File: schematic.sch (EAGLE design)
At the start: 32 parts, among them IC1 PIC16F877P, T1 2N2222, T2 2N2222

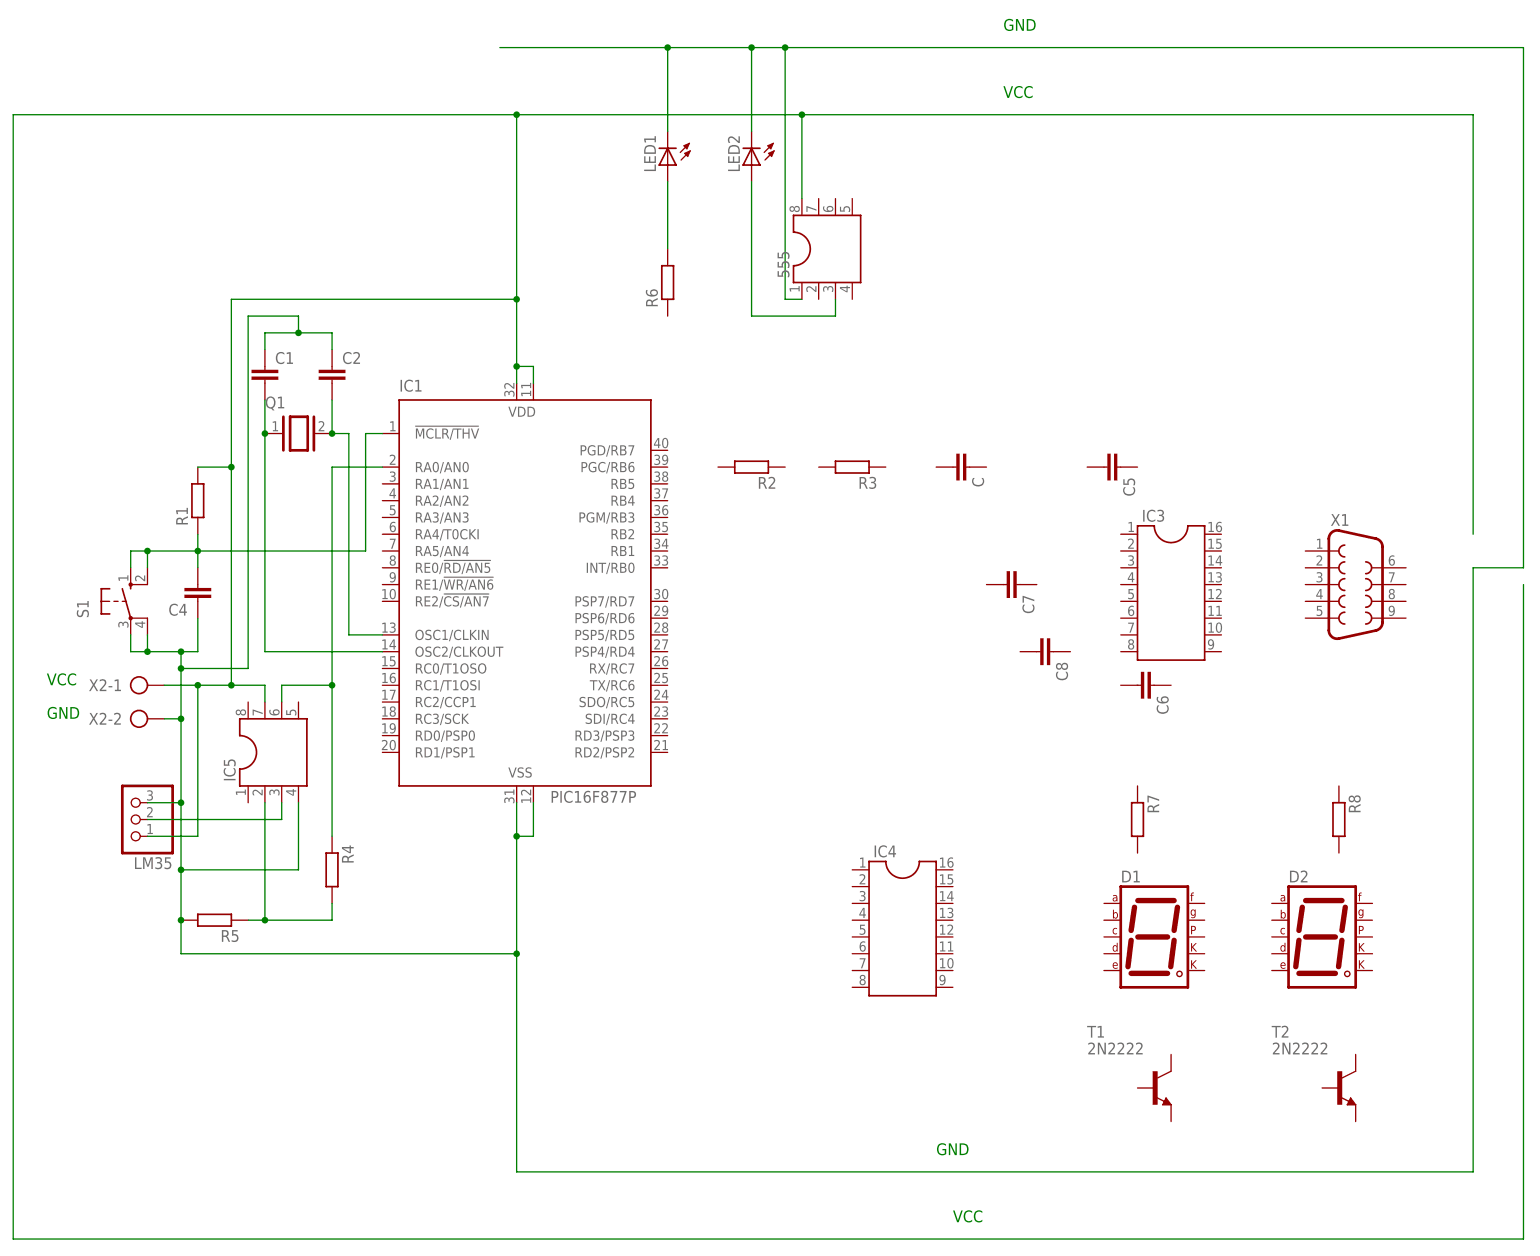
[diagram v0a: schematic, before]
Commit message: choix final du modele du pic + ajout de 4 condo max232 + suite schéma
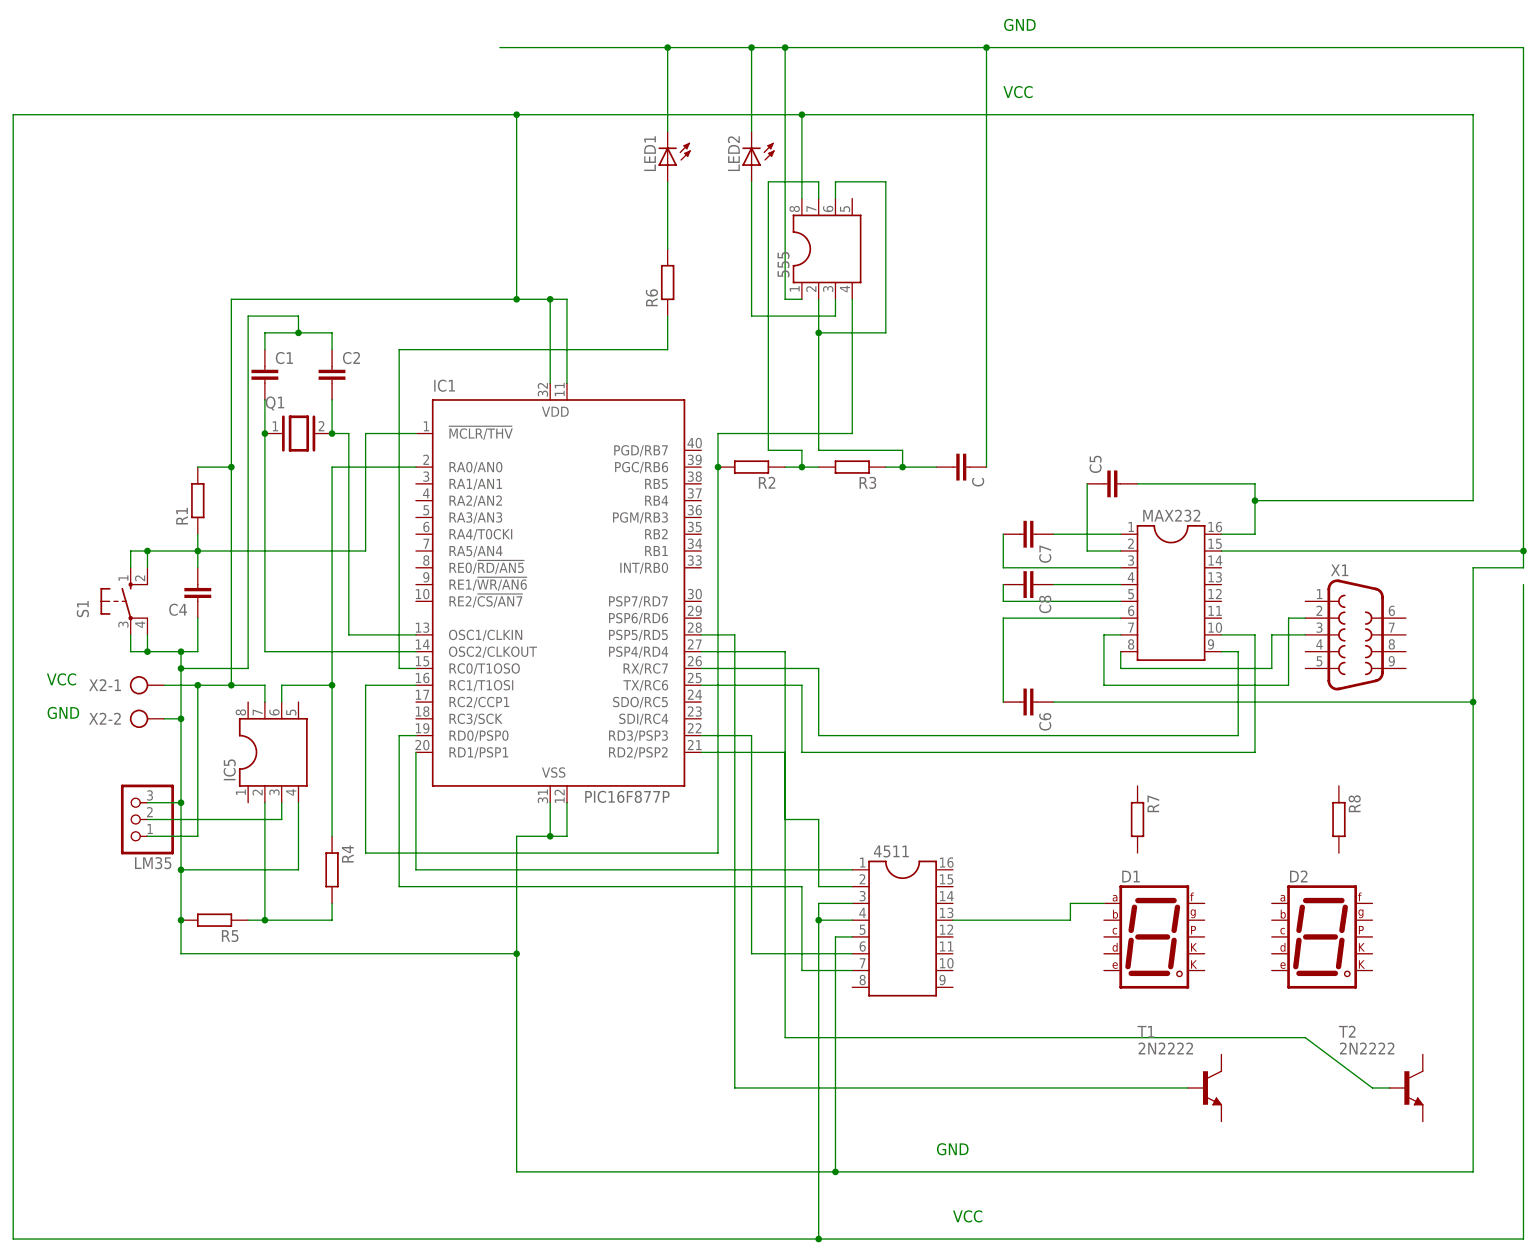
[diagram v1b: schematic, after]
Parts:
- renumbered IC3 to MAX232, IC4 to 4511
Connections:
- removed net N$1: 555.8, IC1.VDD, IC1.VDD@1, IC5.7, LM35.1, R1.2, X2-1.KL
- new net N$12: 555.2, 555.6, C.2, R3.1
- new net N$13: IC1.RC0/T1OSO, R6.1
- new net N$14: 555.4, IC1.RC1/T1OSI, R2.2
- new net N$15: MAX232.7, X1.2
- new net N$16: MAX232.8, X1.3
- new net N$17: C5.1, MAX232.2
- new net N$18: C7.1, MAX232.1
- new net N$19: C7.2, MAX232.3
- new net N$20: C8.1, MAX232.4
- new net N$21: C8.2, MAX232.5
- new net N$22: C6.2, MAX232.6
- new net N$23: IC1.TX/RC6, MAX232.10
- new net N$24: IC1.RX/RC7, MAX232.9
- new net N$25: 555.7, R2.1, R3.2
- new net N$26: 4511.7, IC1.RD0/PSP0
- new net N$27: 4511.3, 4511.4, 555.8, C5.2, IC1.VDD, IC1.VDD@1, IC5.7, LM35.1, MAX232.16, R1.2, X2-1.KL
- new net N$28: 4511.2, IC1.RD2/PSP2
- new net N$29: 4511.6, IC1.RD3/PSP3
- new net N$30: IC1.PSP4/RD4, T2.B
- new net N$31: IC1.PSP5/RD5, T1.B
- new net N$32: 4511.13, D1.A
- new net N$9: 4511.1, IC1.RD1/PSP1
- net N$6: now also 4511.5, C.1, C6.1, MAX232.15
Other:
- moved on the sheet: C5, C6, C7, C8, IC1, T1, T2, X1

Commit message: end of schematic connection 7seg finie
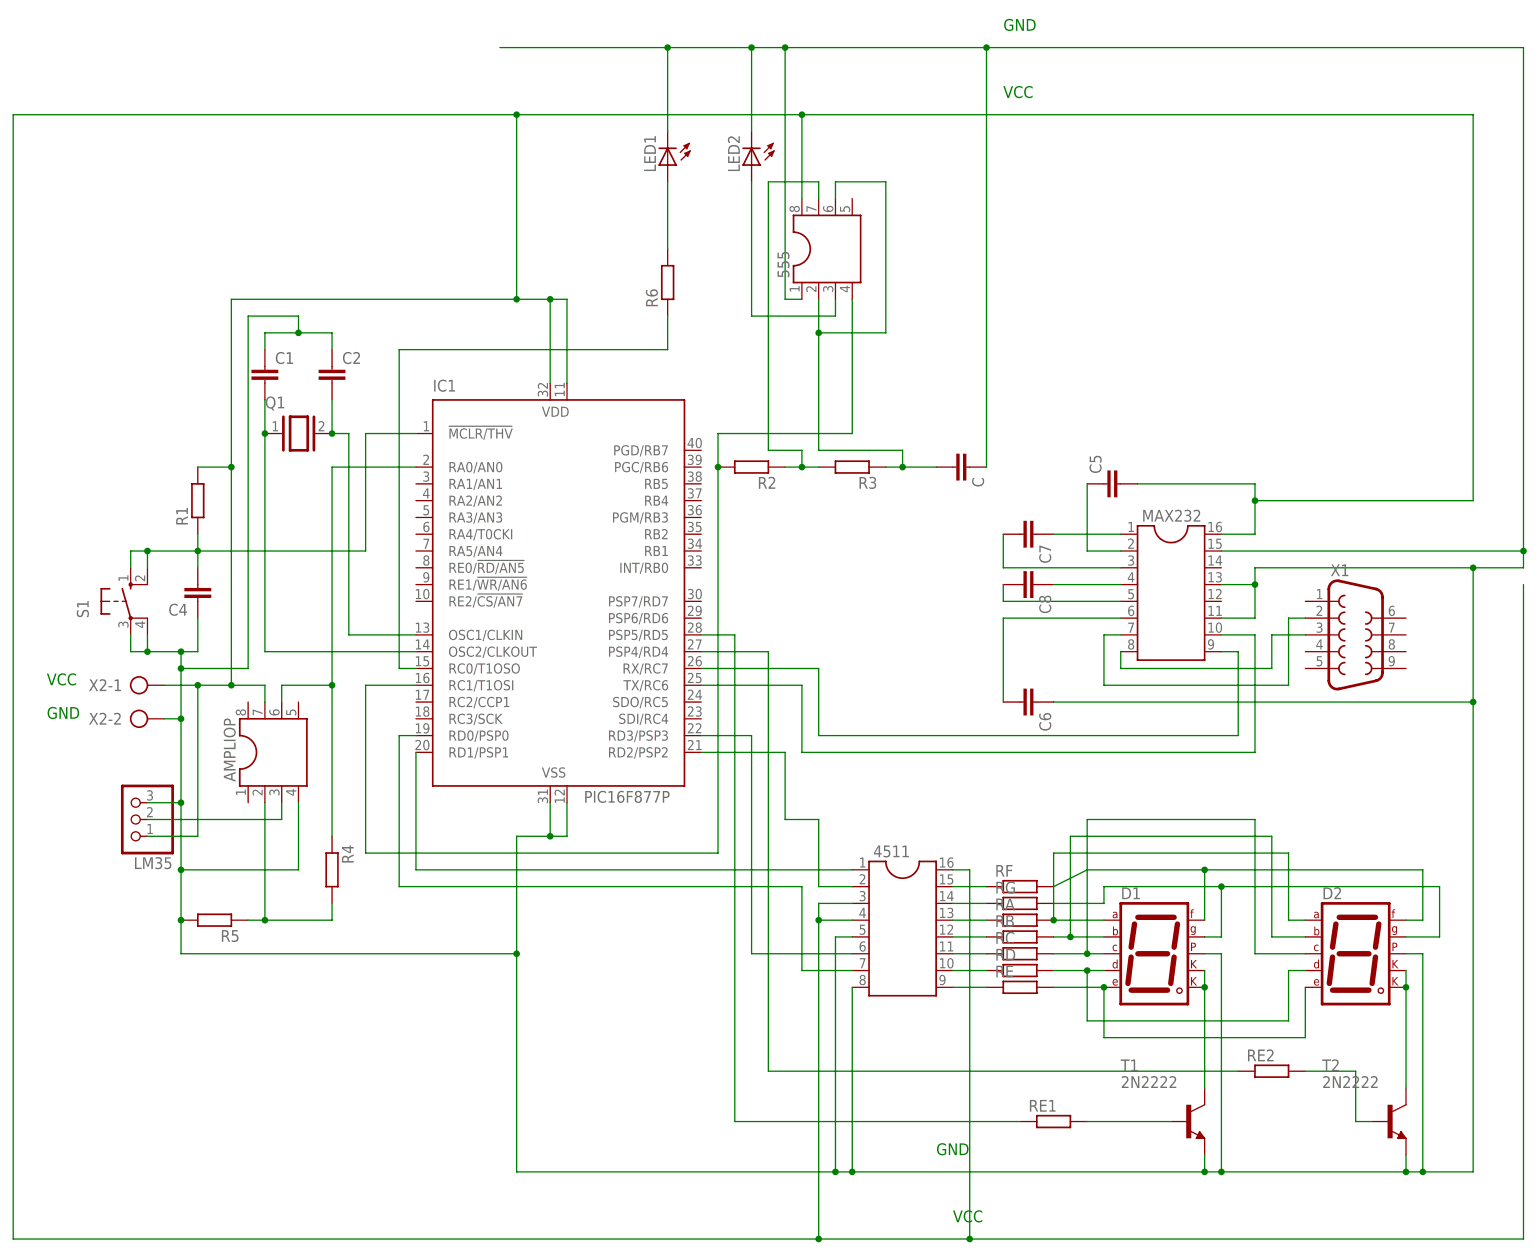
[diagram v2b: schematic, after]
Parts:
- removed R7, R8: (no value), rcl:R-EU_0617/22
- added RA, RB, RC, RD, RE, RE1, RE2, RF, RG: (no value), rcl:R-EU_0617/22
- renumbered IC5 to AMPLIOP
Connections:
- removed net N$6: 4511.5, 555.1, AMPLIOP.4, C.1, C1.1, C2.1, C4.1, C6.1, IC1.VSS, IC1.VSS@1, LED1.C, LED2.C, LM35.3, MAX232.15, R5.2, S1.P, S1.P1, X2-2.KL
- new net N$1: IC1.PSP4/RD4, RE2.1
- new net N$33: 4511.11, RC.1
- new net N$34: 4511.10, RD.1
- new net N$35: 4511.9, RE.1
- new net N$36: D1.A, D2.A, RA.2
- new net N$37: D1.B, D2.B, RB.2
- new net N$38: D1.C, D2.C, RC.2
- new net N$39: D1.D, D2.D, RD.2
- new net N$40: D1.E, D2.E, RE.2
- new net N$41: 4511.15, RF.1
- new net N$42: 4511.14, RG.1
- new net N$43: D1.F, D2.F, RF.2
- new net N$44: D1.G, D2.G, RG.2
- new net N$45: RE1.2, T1.B
- new net N$46: 4511.16, 4511.3, 4511.4, 555.8, AMPLIOP.7, C5.2, IC1.VDD, IC1.VDD@1, LM35.1, MAX232.16, R1.2, X2-1.KL
- new net N$47: D2.CK1, D2.CK2, T2.C
- new net N$48: RE2.2, T2.B
- new net N$49: 4511.5, 4511.8, 555.1, AMPLIOP.4, C.1, C1.1, C2.1, C4.1, C6.1, D1.DP, D2.DP, IC1.VSS, IC1.VSS@1, LED1.C, LED2.C, LM35.3, MAX232.11, MAX232.13, MAX232.15, R5.2, S1.P, S1.P1, T1.E, T2.E, X2-2.KL
- net N$27: now also D1.CK1, D1.CK2, T1.C; no longer 4511.3, 4511.4, 555.8, AMPLIOP.7, C5.2, IC1.VDD, IC1.VDD@1, LM35.1, MAX232.16, R1.2, X2-1.KL
- net N$30: now also 4511.13, RA.1; no longer IC1.PSP4/RD4, T2.B
- net N$31: now also RE1.1; no longer T1.B
- net N$32: now also 4511.12, RB.1; no longer 4511.13, D1.A
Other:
- moved on the sheet: D1, D2, T1, T2

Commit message: schematic to pcb done 10% routing
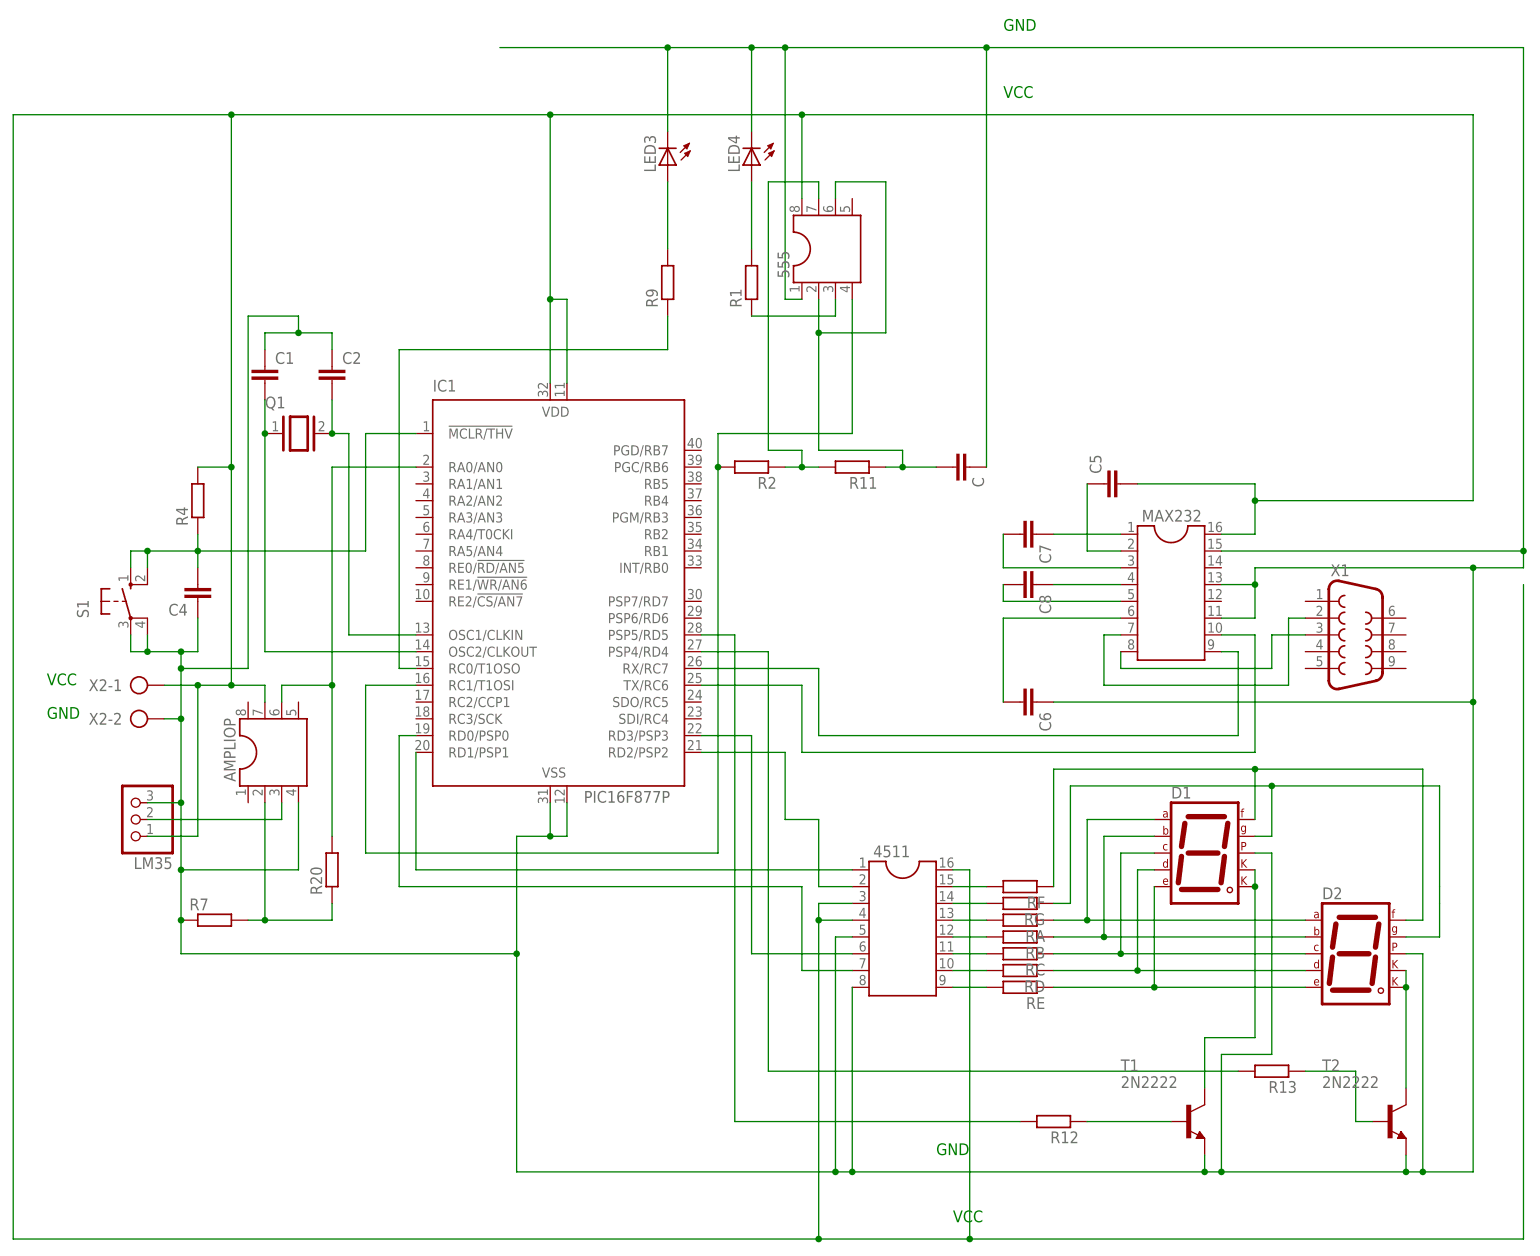
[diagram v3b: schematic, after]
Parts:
- removed LED1, LED2: (no value), eagle-ltspice:LED_E
- removed R3, R5, R6, RE1, RE2: (no value), rcl:R-EU_0617/22
- added LED3, LED4: (no value), eagle-ltspice:LED_ELD260
- added R11, R12, R13, R20, R7, R9: (no value), rcl:R-EU_0204/7
- R1, R2, R4, RA, RB, RC, RD, RE, RF, RG: device rcl:R-EU_0617/22 -> rcl:R-EU_0204/7
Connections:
- removed net N$43: D1.F, D2.F, RF.2
- removed net N$49: 4511.5, 4511.8, 555.1, AMPLIOP.4, C.1, C1.1, C2.1, C4.1, C6.1, D1.DP, D2.DP, IC1.VSS, IC1.VSS@1, LED1.C, LED2.C, LM35.3, MAX232.11, MAX232.13, MAX232.15, R5.2, S1.P, S1.P1, T1.E, T2.E, X2-2.KL
- new net N$51: D1.B, D2.B, RB.1
- new net N$53: D1.F, D2.F, RF.1
- new net N$6: LED4.A, R1.2
- net N$1: now also R13.2; no longer RE2.1
- net N$10: now also LED3.A, R9.2; no longer LED1.A, R6.2
- net N$11: now also R1.1; no longer LED2.A
- net N$12: now also R11.1; no longer R3.1
- net N$13: now also R9.1; no longer R6.1
- net N$25: now also R11.2; no longer R3.2
- net N$3: now also R20.1, R7.2; no longer R4.2, R5.1
- net N$30: now also RA.2; no longer RA.1
- net N$31: now also R12.2; no longer RE1.1
- net N$32: now also RB.2; no longer RB.1
- net N$33: now also RC.2; no longer RC.1
- net N$34: now also RD.2; no longer RD.1
- net N$35: now also RE.2; no longer RE.1
- net N$36: now also RA.1; no longer RA.2
- net N$37: now also D1.D, D2.D, RD.1; no longer D1.B, D2.B, RB.2
- net N$38: now also RC.1; no longer RC.2
- net N$39: now also D1.E, D2.E, RE.1; no longer D1.D, D2.D, RD.2
- net N$4: now also R20.2; no longer R4.1
- net N$40: now also 4511.5, 4511.8, 555.1, AMPLIOP.4, C.1, C1.1, C2.1, C4.1, C6.1, D1.DP, D2.DP, IC1.VSS, IC1.VSS@1, LED3.C, LED4.C, LM35.3, MAX232.11, MAX232.13, MAX232.15, R7.1, S1.P, S1.P1, T1.E, T2.E, X2-2.KL; no longer D1.E, D2.E, RE.2
- net N$41: now also RF.2; no longer RF.1
- net N$42: now also RG.2; no longer RG.1
- net N$44: now also RG.1; no longer RG.2
- net N$45: now also R12.1; no longer RE1.2
- net N$46: now also R4.2; no longer R1.2
- net N$48: now also R13.1; no longer RE2.2
- net N$7: now also R4.1; no longer R1.1
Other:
- moved on the sheet: D1, R1, R4, RA, RB, RC, RD, RE, RF, RG

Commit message: correction to board + plan de masse
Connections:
- net N$40 renamed GND
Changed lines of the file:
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@@
 <setting verticaltext="up"/>
 </settings>
-<grid distance="0.1" unitdist="inch" unit="inch" style="lines" multiple="1" display="yes" altdistance="0.01" altunitdist="inch" altunit="inch"/>
+<grid distance="0.1" unitdist="inch" unit="inch" style="lines" multiple="1" display="no" altdistance="0.01" altunitdist="inch" altunit="inch"/>
 <layers>
 <layer number="1" name="Top" color="4" fill="1" visible="no" active="no"/>
@@
 </segment>
 </net>
-<net name="N$40" class="0">
+<net name="GND" class="0">
 <segment>
 <pinref part="D1" gate="G$1" pin="DP"/>
